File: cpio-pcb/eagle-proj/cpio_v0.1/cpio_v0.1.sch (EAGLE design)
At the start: 60 parts

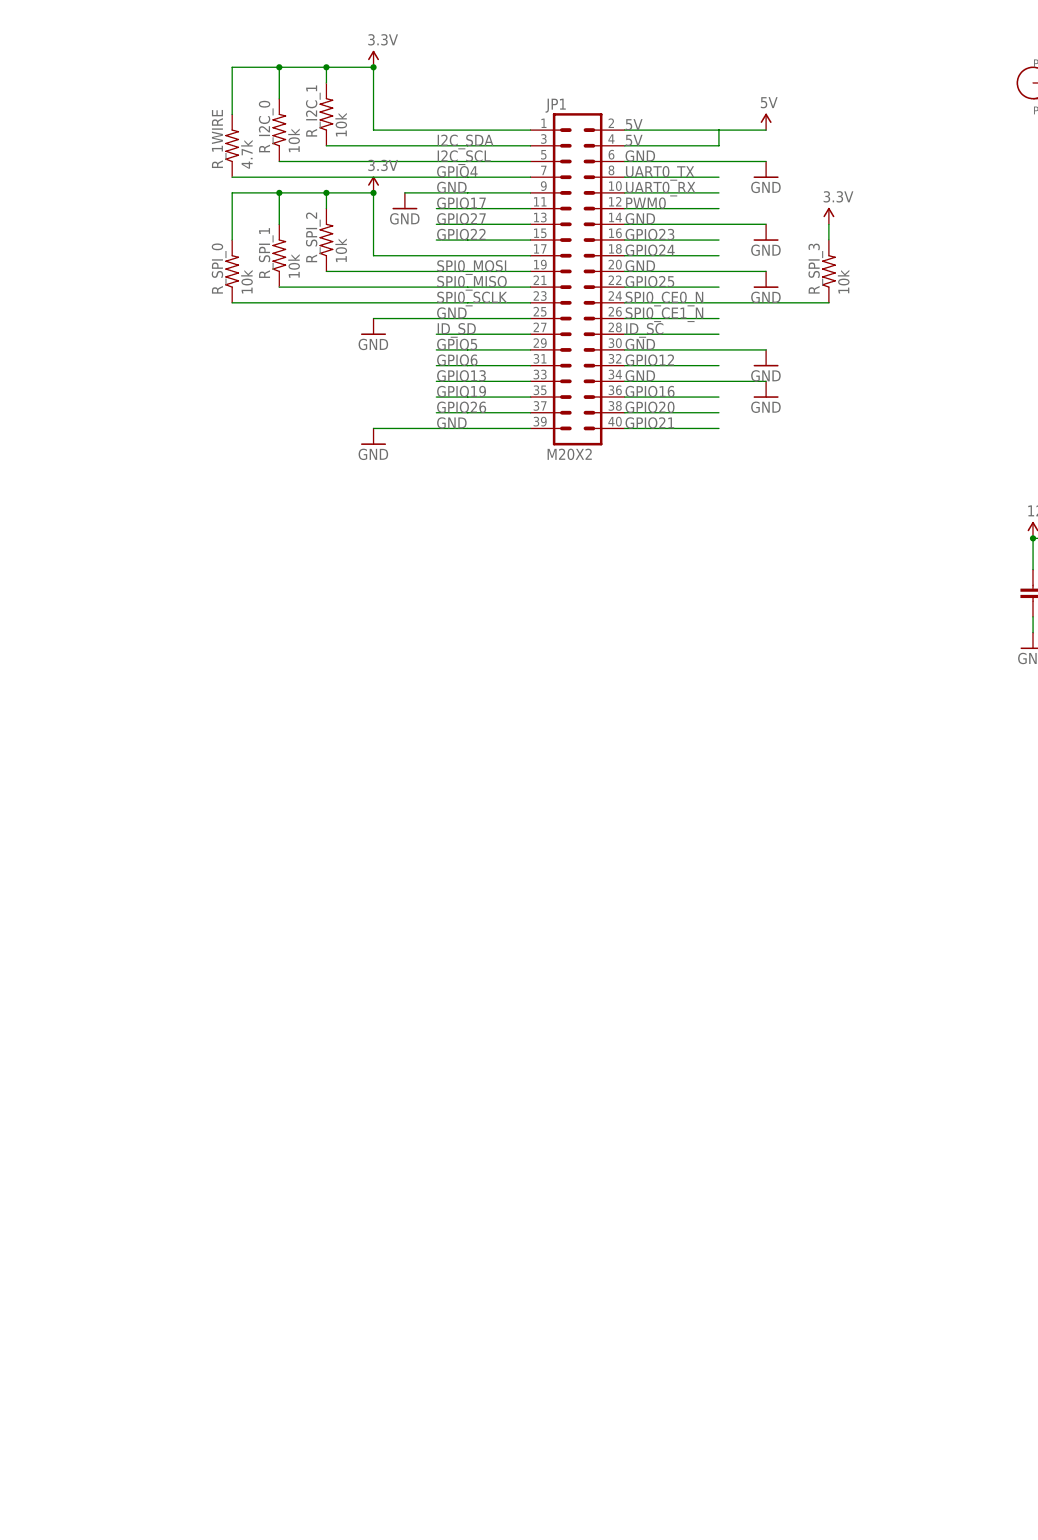
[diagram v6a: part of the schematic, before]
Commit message: RGB LEDs added to schematic
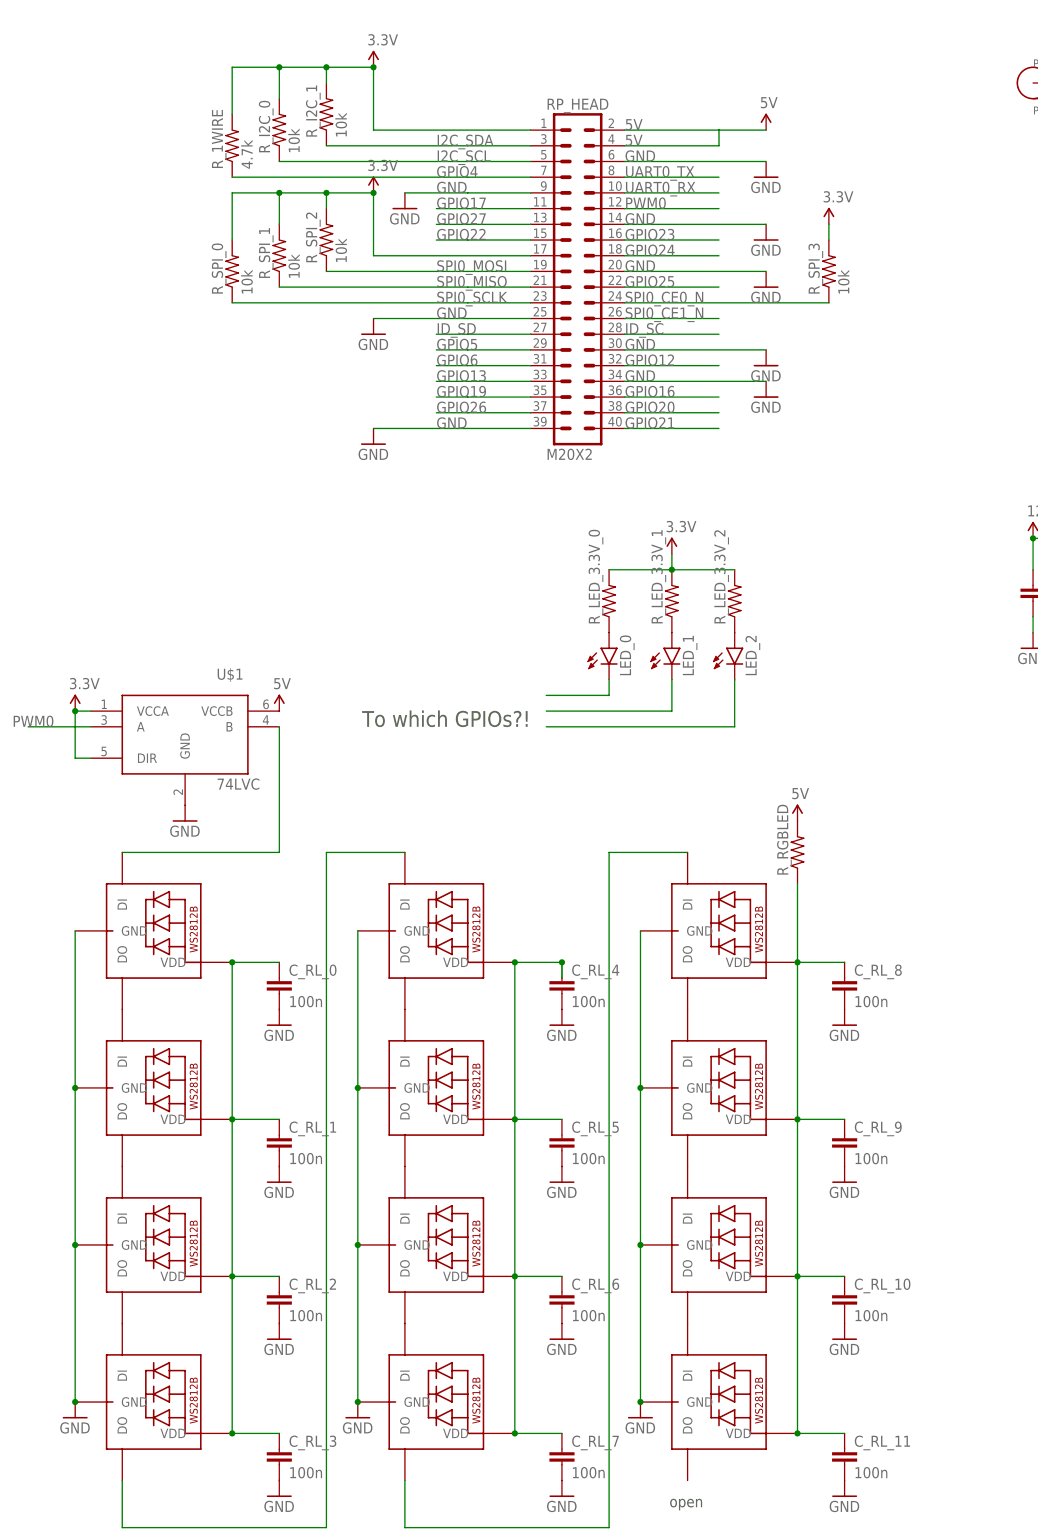
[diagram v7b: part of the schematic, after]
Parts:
- added C_RL_0, C_RL_1, C_RL_10, C_RL_11, C_RL_2, C_RL_3, C_RL_4, C_RL_5, C_RL_6, C_RL_7, C_RL_8, C_RL_9: 100n, SparkFun-Passives:CAP0805
- added LED_0, LED_1, LED_2: (no value), SparkFun-LED:LED1206
- added RL_BRIGHT, RL_CAMERA, RL_HEAT_0, RL_HEAT_1, RL_HEAT_2, RL_HEAT_3, RL_HUM_0, RL_HUM_1, RL_TEMP_0, RL_TEMP_1, RL_TEMP_2, RL_TEMP_3: WS2812B5050, adafruit:WS2812B5050
- added R_LED_3.3V_0, R_LED_3.3V_1, R_LED_3.3V_2, R_RGBLED: (no value), SparkFun-Passives:RESISTOR0805-RES
- added U$1: 74LVC, cpio:74LVC
- renumbered JP1 to RP_HEAD
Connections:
- new net N$43: RL_HEAT_2.DO, RL_HEAT_3.DI
- new net N$44: RL_HEAT_1.DO, RL_HEAT_2.DI
- new net N$45: RL_HEAT_0.DO, RL_HEAT_1.DI
- new net N$46: RL_TEMP_2.DO, RL_TEMP_3.DI
- new net N$47: RL_TEMP_1.DO, RL_TEMP_2.DI
- new net N$48: RL_TEMP_0.DO, RL_TEMP_1.DI
- new net N$49: RL_BRIGHT.DO, RL_CAMERA.DI
- new net N$50: RL_BRIGHT.DI, RL_HUM_1.DO
- new net N$51: RL_HUM_0.DO, RL_HUM_1.DI
- new net N$52: C_RL_10.1, C_RL_11.1, C_RL_8.1, C_RL_9.1, RL_BRIGHT.VDD, RL_CAMERA.VDD, RL_HUM_0.VDD, RL_HUM_1.VDD, R_RGBLED.1
- new net N$53: RL_HEAT_0.DI, U$1.B
- new net N$54: LED_0.A, R_LED_3.3V_0.1
- new net N$55: LED_1.A, R_LED_3.3V_1.1
- new net N$56: LED_2.A, R_LED_3.3V_2.1
- new net N$58: RL_HUM_0.DI, RL_TEMP_3.DO
- new net N$59: RL_HEAT_3.DO, RL_TEMP_0.DI
- new net N$60: LED_0.C
- new net N$61: C_RL_4.1, C_RL_5.1, C_RL_6.1, C_RL_7.1, RL_TEMP_0.VDD, RL_TEMP_1.VDD, RL_TEMP_2.VDD, RL_TEMP_3.VDD
- new net N$62: LED_1.C
- new net N$63: LED_2.C
- new net N$67: C_RL_0.1, C_RL_1.1, C_RL_2.1, C_RL_3.1, RL_HEAT_0.VDD, RL_HEAT_1.VDD, RL_HEAT_2.VDD, RL_HEAT_3.VDD
- net 3.3V: now also R_LED_3.3V_0.2, R_LED_3.3V_1.2, R_LED_3.3V_2.2, U$1.DIR, U$1.VCCA
- net 5V: now also R_RGBLED.2, U$1.VCCB
- net GND: now also C_RL_0.2, C_RL_1.2, C_RL_10.2, C_RL_11.2, C_RL_2.2, C_RL_3.2, C_RL_4.2, C_RL_5.2, C_RL_6.2, C_RL_7.2, C_RL_8.2, C_RL_9.2, RL_BRIGHT.GND, RL_CAMERA.GND, RL_HEAT_0.GND, RL_HEAT_1.GND, RL_HEAT_2.GND, RL_HEAT_3.GND, RL_HUM_0.GND, RL_HUM_1.GND, RL_TEMP_0.GND, RL_TEMP_1.GND, RL_TEMP_2.GND, RL_TEMP_3.GND, U$1.GND
- net PWM0: now also U$1.A

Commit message: RGB LEDs added to schematic done
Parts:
- added BEEP: BEEPER, cpio:BEEPER
- added PUSH: BUTTON, cpio:BUTTON
- added R_LED_3.3V1, R_PUSHBUT: (no value), SparkFun-Passives:RESISTOR0805-RES
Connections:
- removed net N$7: R_LED_5V.2
- new net N$57: PUSH.P$2, R_PUSHBUT.1
- new net N$64: BEEP.+, R_LED_3.3V1.1
- new net N$65: BEEP.-
- new net N$66: PUSH.P$1
- net 3.3V: now also R_LED_3.3V1.2, R_PUSHBUT.2
- net 5V: now also R_LED_5V.2
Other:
- moved on the sheet: ADC, CAMERA, C_ADC, HEAT_0, HEAT_1, HEAT_2, HEAT_3, LED_0, LED_1, LED_2, R_BRIGHT, R_HSS_GND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
